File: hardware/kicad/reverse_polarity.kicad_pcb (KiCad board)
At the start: 2 copper layers, 32.5 x 36.7 mm, 15 parts, among them J1 12V_IN, J2 12V_IN, Q1 IRF4905

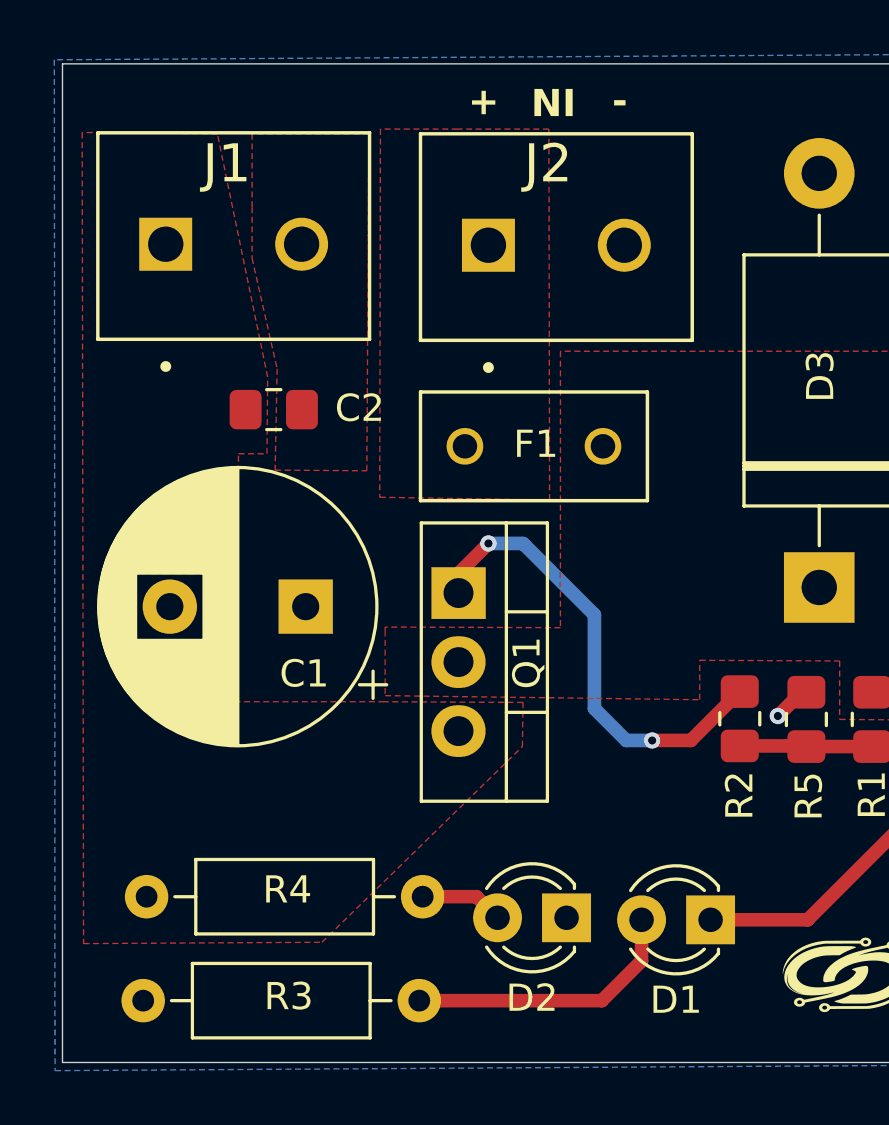
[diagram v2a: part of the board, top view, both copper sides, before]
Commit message: docs: added bom, 3d & prints(pcb) - reverse polarity
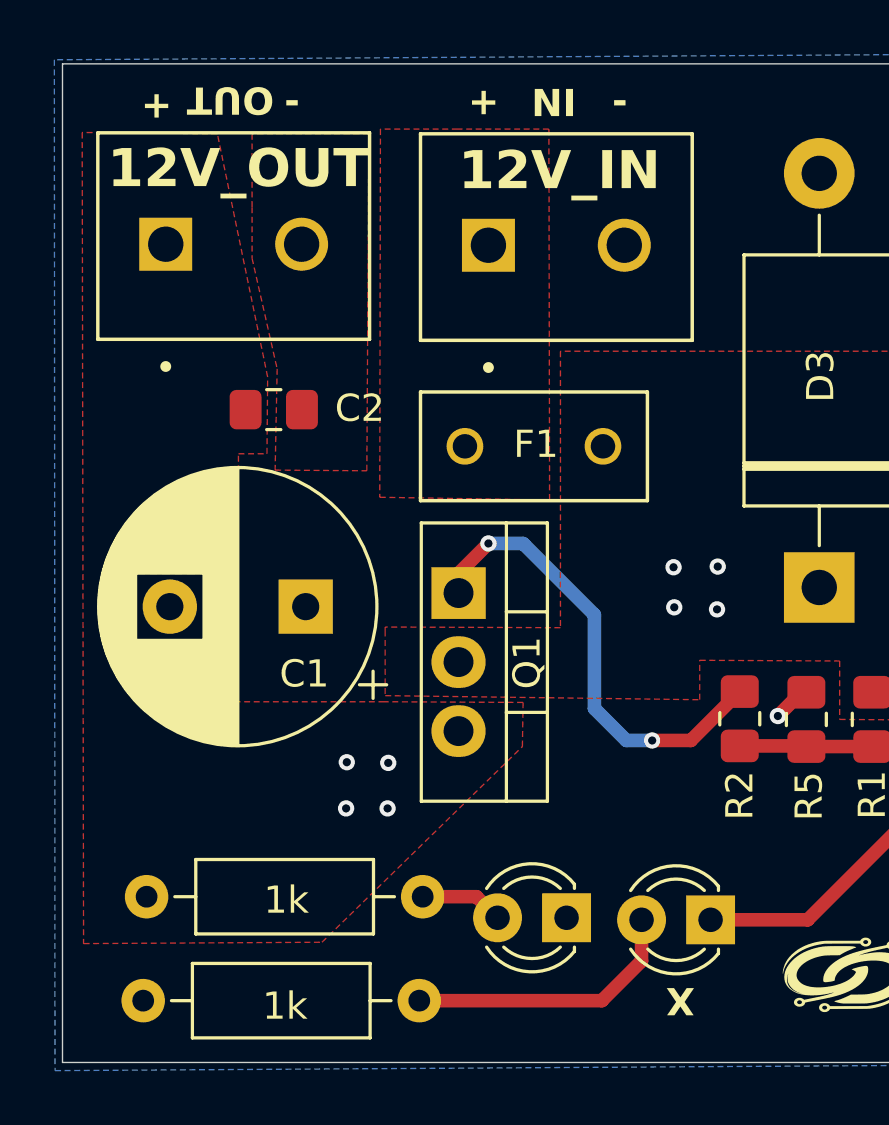
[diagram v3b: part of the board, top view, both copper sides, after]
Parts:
- J1: value 12V_IN -> 12V_OUT
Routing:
- net /V12_PROT: vias 0 -> 4
- net /V12_FUSED: vias 0 -> 4
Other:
- board text added: "OUT"
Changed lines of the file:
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@@
     (property "ki_keywords" "screw terminal")
     (attr through_hole)
-    (fp_text reference "J2" (at 2.2 -3) (layer "F.SilkS")
+    (fp_text reference "J2" (at 2.2 -3) (layer "F.SilkS") hide
         (effects (font (size 1.4 1.4) (thickness 0.15)))
     )
-    (fp_text value "12V_IN" (at 12.502 4.861) (layer "F.Fab")
-        (effects (font (size 1.4 1.4) (thickness 0.15)))
+    (fp_text value "12V_IN" (at 2.6125 -2.75) (layer "F.SilkS")
+        (effects (font (size 1.4 1.4) (thickness 0.28) bold))
     )
     (fp_line (start -2.5 -4.1) (end 7.5 -4.1)
@@
     (property "ki_keywords" "screw terminal")
     (attr through_hole)
-    (fp_text reference "J1" (at 2.25 -2.9625) (layer "F.SilkS")
+    (fp_text reference "J1" (at 2.25 -2.9625) (layer "F.SilkS") hide
         (effects (font (size 1.4 1.4) (thickness 0.15)))
     )
-    (fp_text value "12V_IN" (at 12.502 4.861) (layer "F.Fab")
-        (effects (font (size 1.4 1.4) (thickness 0.15)))
+    (fp_text value "12V_OUT" (at 2.6625 -2.7875) (layer "F.SilkS")
+        (effects (font (size 1.4 1.4) (thickness 0.28) bold))
     )
     (fp_line (start -2.5 -4.1) (end 7.5 -4.1)
@@
     (property "ki_keywords" "R res resistor")
     (attr through_hole)
-    (fp_text reference "R3" (at 5.355 -0.15) (layer "F.SilkS")
-        (effects (font (size 1 1) (thickness 0.15)))
-    )
-    (fp_text value "1k" (at 5.08 2.37) (layer "F.Fab")
+    (fp_text reference "R3" (at 5.355 -0.15) (layer "F.SilkS") hide
+        (effects (font (size 1 1) (thickness 0.15)))
+    )
+    (fp_text value "1k" (at 5.2175 0.2) (layer "F.SilkS")
         (effects (font (size 1 1) (thickness 0.15)))
     )
@@
     (property "ki_keywords" "LED diode")
     (attr through_hole)
-    (fp_text reference "D1" (at 1.27 -2.96) (layer "F.SilkS")
+    (fp_text reference "D1" (at 1.27 -2.96) (layer "F.SilkS") hide
         (effects (font (size 1 1) (thickness 0.15)))
     )
     (fp_text value "RED" (at 1.27 2.96) (layer "F.Fab")
         (effects (font (size 1 1) (thickness 0.15)))
+    )
+    (fp_text user "X" (at 1.1125 -2.975 180 unlocked) (layer "F.SilkS")
+        (effects (font (size 1 1) (thickness 0.2) bold))
     )
     (fp_line (start -0.29 -1.236) (end -0.29 -1.08)
@@
     (property "ki_keywords" "R res resistor")
     (attr through_hole)
-    (fp_text reference "R4" (at 5.18 -0.25) (layer "F.SilkS")
-        (effects (font (size 1 1) (thickness 0.15)))
-    )
-    (fp_text value "1k" (at 5.08 2.37) (layer "F.Fab")
+    (fp_text reference "R4" (at 5.18 -0.25) (layer "F.SilkS") hide
+        (effects (font (size 1 1) (thickness 0.15)))
+    )
+    (fp_text value "1k" (at 5.1425 0.125) (layer "F.SilkS")
         (effects (font (size 1 1) (thickness 0.15)))
     )
@@
     (property "ki_keywords" "LED diode")
     (attr through_hole)
-    (fp_text reference "D2" (at 1.27 -2.96) (layer "F.SilkS")
+    (fp_text reference "D2" (at 1.27 -2.96) (layer "F.SilkS") hide
         (effects (font (size 1 1) (thickness 0.15)))
     )
@@
   (gr_rect (start 62.3875 36.225) (end 94.8375 72.975)
     (stroke (width 0.05) (type default)) (fill none) (layer "Edge.Cuts"))
-  (gr_text "IN\n" (at 81.2875 37.025 180) (layer "F.SilkS")
+  (gr_text "IN\n" (at 81.3 37.025 180) (layer "F.SilkS")
     (effects (font (size 1 1) (thickness 0.2) bold) (justify left bottom))
   )
@@
     (effects (font (size 1 1) (thickness 0.2) bold) (justify left bottom))
   )
+  (gr_text "-" (at 70.55 38.175) (layer "F.SilkS")
+    (effects (font (size 1 1) (thickness 0.2) bold) (justify left bottom))
+  )
+  (gr_text "+" (at 65.275 38.325) (layer "F.SilkS")
+    (effects (font (size 1 1) (thickness 0.2) bold) (justify left bottom))
+  )
   (gr_text "-" (at 82.6125 38.175) (layer "F.SilkS")
+    (effects (font (size 1 1) (thickness 0.2) bold) (justify left bottom))
+  )
+  (gr_text "OUT" (at 70.175 36.975 180) (layer "F.SilkS")
     (effects (font (size 1 1) (thickness 0.2) bold) (justify left bottom))
   )
@@
   (segment (start 89.7625 59.35) (end 89.5875 59.35) (width 0.5) (layer "F.Cu") (net 1))
   (via (at 88.7125 60.225) (size 0.6) (drill 0.3) (layers "F.Cu" "B.Cu") (net 1))
+  (via (at 74.375 61.95) (size 0.6) (drill 0.3) (layers "F.Cu" "B.Cu") (free) (net 2))
+  (via (at 74.35 63.625) (size 0.6) (drill 0.3) (layers "F.Cu" "B.Cu") (free) (net 2))
+  (via (at 72.85 61.925) (size 0.6) (drill 0.3) (layers "F.Cu" "B.Cu") (free) (net 2))
+  (via (at 72.825 63.625) (size 0.6) (drill 0.3) (layers "F.Cu" "B.Cu") (free) (net 2))
   (segment (start 82.2375 70.7) (end 83.6975 69.24) (width 0.5) (layer "F.Cu") (net 3))
   (segment (start 75.5175 70.7) (end 82.2375 70.7) (width 0.5) (layer "F.Cu") (net 3))
@@
   (segment (start 92.9625 59.35) (end 93.7375 60.125) (width 0.5) (layer "F.Cu") (net 8))
   (segment (start 92.1875 59.35) (end 92.9625 59.35) (width 0.5) (layer "F.Cu") (net 8))
+  (via (at 84.875 54.75) (size 0.6) (drill 0.3) (layers "F.Cu" "B.Cu") (free) (net 8))
+  (via (at 86.475 56.3) (size 0.6) (drill 0.3) (layers "F.Cu" "B.Cu") (free) (net 8))
+  (via (at 84.9 56.225) (size 0.6) (drill 0.3) (layers "F.Cu" "B.Cu") (free) (net 8))
+  (via (at 86.5 54.725) (size 0.6) (drill 0.3) (layers "F.Cu" "B.Cu") (free) (net 8))
   (zone (net 2) (net_name "/V12_PROT") (layer "F.Cu") (name "VOUT") (hatch edge 0.5)
     (priority 3)
     (connect_pads (clearance 0.3))
     (min_thickness 0.25) (filled_areas_thickness no)
-    (fill yes (thermal_gap 0.5) (thermal_bridge_width 0.5))
+    (fill yes (thermal_gap 0.5) (thermal_bridge_width 0.8))
     (polygon
       (pts
@@
     (connect_pads (clearance 0.3))
     (min_thickness 0.25) (filled_areas_thickness no)
-    (fill yes (thermal_gap 0.5) (thermal_bridge_width 0.5))
+    (fill yes (thermal_gap 0.5) (thermal_bridge_width 0.8))
     (polygon
       (pts
@@
     (connect_pads (clearance 0.3))
     (min_thickness 0.25) (filled_areas_thickness no)
-    (fill yes (thermal_gap 0.5) (thermal_bridge_width 0.5))
+    (fill yes (thermal_gap 0.5) (thermal_bridge_width 0.8))
     (polygon
       (pts
